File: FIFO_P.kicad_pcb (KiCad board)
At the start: 4 copper layers, 100 x 100 mm, 74 parts, among them J1 Vin +, J2 Vin -, J3 ICLK, J4 Vout, J5 Jack-DC, SW1 Rotary_Encoder_61C, U1 SN74LVC2G157_MUX_TI, U10 AD7840, U11 LM2776, U12 LM2940CT-5.0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

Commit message: Moved power
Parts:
- moved R2 15.4 mm to (91.5, 63.2), turned to 90 degrees
- moved JP2 13.5 mm to (118.0, 76.8), turned to 180 degrees
- moved R1 11.1 mm to (93.5, 63.2), turned to 90 degrees
- moved C20 11.0 mm to (66.5, 88.2)
- moved C21 11.0 mm to (66.5, 78.5)
- moved C22 11.0 mm to (66.5, 81.5)
- moved C25 11.0 mm to (77.2, 89.0)
- moved C26 11.0 mm to (66.5, 94.2)
- moved C27 11.0 mm to (80.2, 89.0)
- moved C28 11.0 mm to (66.5, 91.2)
- moved C29 11.0 mm to (66.5, 100.2)
- moved C30 11.0 mm to (66.5, 97.2)
- moved C31 11.0 mm to (85.8, 89.0)
- moved TP5 11.0 mm to (65.2, 85.0)
- moved TP6 11.0 mm to (92.5, 89.0)
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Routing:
- net Net-(C21-Pad1): track 34.3 -> 28.6 mm
- net -5V: track 183.2 -> 179.0 mm
- net +5V: track 225.8 -> 222.8 mm
- net GNDA: track 20.8 -> 17.8 mm
- net Net-(J2-Pad1): track 18.4 -> 19.6 mm
- net Net-(J1-Pad1): track 15.4 -> 16.6 mm
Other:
- board size 100 x 100 mm -> 95 x 100 mm
- board text added: "TODO {Non-,}differential signaling switch? Perfectly center traces between pins (where app.)? Silkscreen Check Soldermask Expansion Check Move power, reshape board: check Ard. stickout"
- board text removed: "TODO Extend SMD footprints {Non-,}differential signaling switch Center traces between pins Silkscreen Move power, reshape board: check Ard. stickout"

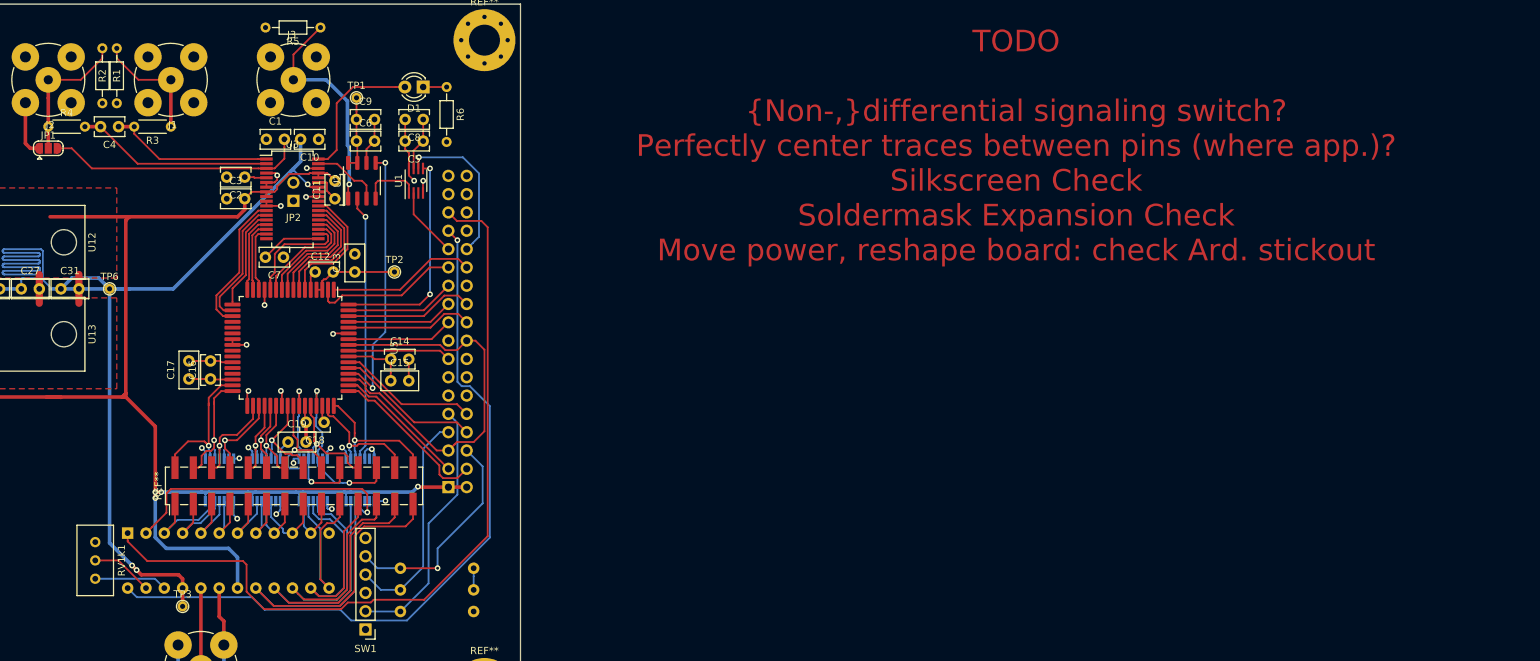
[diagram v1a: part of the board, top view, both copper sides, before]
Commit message: Actually fixed power and clocks
TODO: Flip arduino header and reroute
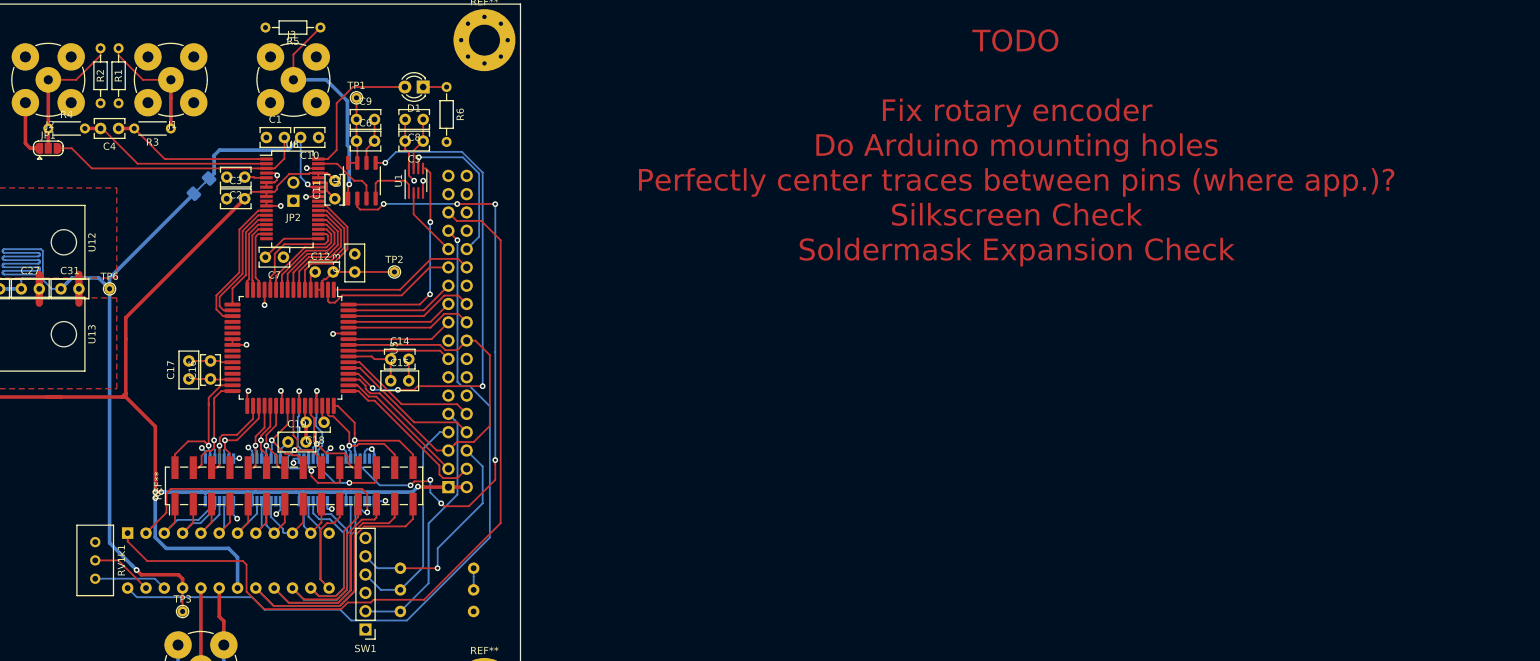
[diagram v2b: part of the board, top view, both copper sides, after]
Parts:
- added REF**: C_1206_3216Metric_Pad1.42x1.75mm_HandSolder, Capacitor_SMD:C_1206_3216Metric_Pad1.42x1.75mm_HandSolder, B.Cu at (105.2, 74.8)
- moved TP3 0.71 mm to (102.6, 133.8)
- moved C1 0.25 mm to (114.2, 68.0)
- moved C10 0.25 mm to (121.5, 68.0)
- moved C4 0.25 mm to (93.8, 66.8)
- moved R1 0.25 mm to (93.8, 63.2)
- moved R2 0.25 mm to (91.2, 63.2)
- moved R3 0.25 mm to (101.0, 66.8)
- moved R4 0.25 mm to (84.0, 66.8)
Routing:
- net LDAC: track 36.9 -> 84.2 mm, vias 1 -> 7
- net RCLK: track 38.7 -> 67.3 mm, vias 2 -> 4
- net +5V: track 222.8 -> 203.0 mm
- net -5V: track 179.0 -> 172.8 mm, vias 3 -> 2
- net Net-(U10-Pad1): track 110.7 -> 112.2 mm
- net Net-(C4-Pad1): track 22.9 -> 22.3 mm
- net Net-(U4-Pad24): track 56.4 -> 57.0 mm
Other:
- board text added: "TODO Fix rotary encoder Do Arduino mounting holes Perfectly center traces between pins (where app.)? Silkscreen Check Soldermask Expansion Check"
- board text removed: "TODO {Non-,}differential signaling switch? Perfectly center traces between pins (where app.)? Silkscreen Check Soldermask Expansion Check Move power, reshape board: check Ard. stickout"

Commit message: Fixed Arduino mounting holes
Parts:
- removed the REF** at (62.5, 71.0)
- added REF**: MountingHole_3.2mm_M3_ISO14580, MountingHole:MountingHole_3.2mm_M3_ISO14580, F.Cu at (60.8, 116.5)
- added REF**: MountingHole_3.2mm_M3_ISO14580, MountingHole:MountingHole_3.2mm_M3_ISO14580, F.Cu at (59.5, 68.2)
- moved REF** 5.00 mm to (54.5, 144.5)
- moved REF** 5.00 mm to (54.5, 54.5)
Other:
- board size 95 x 100 mm -> 100 x 100 mm
- board text added: "TODO Fix rotary encoder Perfectly center traces between pins (where app.)? Silkscreen Check Soldermask Expansion Check"
- board text removed: "TODO Fix rotary encoder Do Arduino mounting holes Perfectly center traces between pins (where app.)? Silkscreen Check Soldermask Expansion Check"

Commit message: Started silkscreen
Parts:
- removed the REF** at (54.5, 54.5)
- added M4: MountingHole_4.3mm_M4_Pad_Via, MountingHole:MountingHole_4.3mm_M4_Pad_Via, F.Cu at (54.5, 54.5)
- moved R5 11.1 mm to (111.0, 55.7), turned to 270 degrees
- moved TP4 7.92 mm to (65.6, 67.5)
- moved SW1 1.00 mm to (128.0, 137.2)
- moved R8 0.34 mm to (142.7, 134.0)
- moved R7 0.28 mm to (142.7, 130.8)
- moved R9 0.26 mm to (142.7, 127.7)
- renumbered REF** to M4
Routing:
- net Net-(U10-Pad1): track 112.2 -> 114.3 mm
- net Net-(R9-Pad2): track 30.5 -> 28.5 mm
- net 3.3V: track 89.4 -> 87.6 mm
- net Net-(U10-Pad24): track 102.5 -> 103.3 mm
- net Net-(J3-Pad1): track 31.2 -> 31.8 mm
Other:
- board text added: "3.3V"
- board text added: "Clock"
- board text added: "Differential Inputs"
- board text added: "Input Overflow"
- board text added: "Short to GND"
- board text removed: "APPROX"

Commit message: Silkscreen cleaned up on both sides
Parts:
- removed the REF** at (59.5, 68.2)
- added M3: MountingHole_3.2mm_M3_ISO14580, MountingHole:MountingHole_3.2mm_M3_ISO14580, F.Cu at (59.5, 68.2)
- moved TP7 1.69 mm to (66.5, 105.2)
- moved R6 1.50 mm to (140.8, 61.0)
- moved JP1 1.25 mm to (84.0, 70.8)
- renumbered REF** to M3
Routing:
- net GND: track 83.8 -> 79.1 mm
- net 3.3V: track 87.6 -> 89.3 mm
- net Net-(D1-Pad1): track 3.31 -> 4.75 mm
- net Net-(J2-Pad1): track 19.1 -> 20.4 mm
- net GNDA: track 17.8 -> 18.4 mm
- net Net-(C1-Pad2): track 36.1 -> 35.6 mm
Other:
- board text added: "+5V"
- board text added: "-5V"
- board text added: "-5V Charge Pump"
- board text added: "ADC"
- board text added: "Arduino Due"
- board text added: "Clock Buffer"
- board text added: "D0"
- board text added: "D13"
- board text added: "DAC"
- board text added: "DAC In"
- board text added: "Delay Adjust"
- board text added: "Delayed Output"
- board text added: "FIFO"
- board text added: "FIFO Out"
- board text added: "Ferrite or Short"
- board text added: "G N D"
- board text added: "GND"
- board text added: "GNDA"
- board text added: "MUX"
- board text added: "Q17"
- board text added: "Q4"
- board text added: "Reference Adjust"
- board text added: "Vin"
- board text added: "a"
- board text added: "b"
- board text added: "c"
- board text removed: "TODO Fix rotary encoder Perfectly center traces between pins (where app.)? Silkscreen Check Soldermask Expansion Check"

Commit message: More tweaks
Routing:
- net LDAC: track 84.2 -> 88.7 mm
- net Net-(R7-Pad2): track 30.6 -> 29.9 mm
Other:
- board text added: "Cut before +ferrite"
- board text removed: "Ferrite or Short"

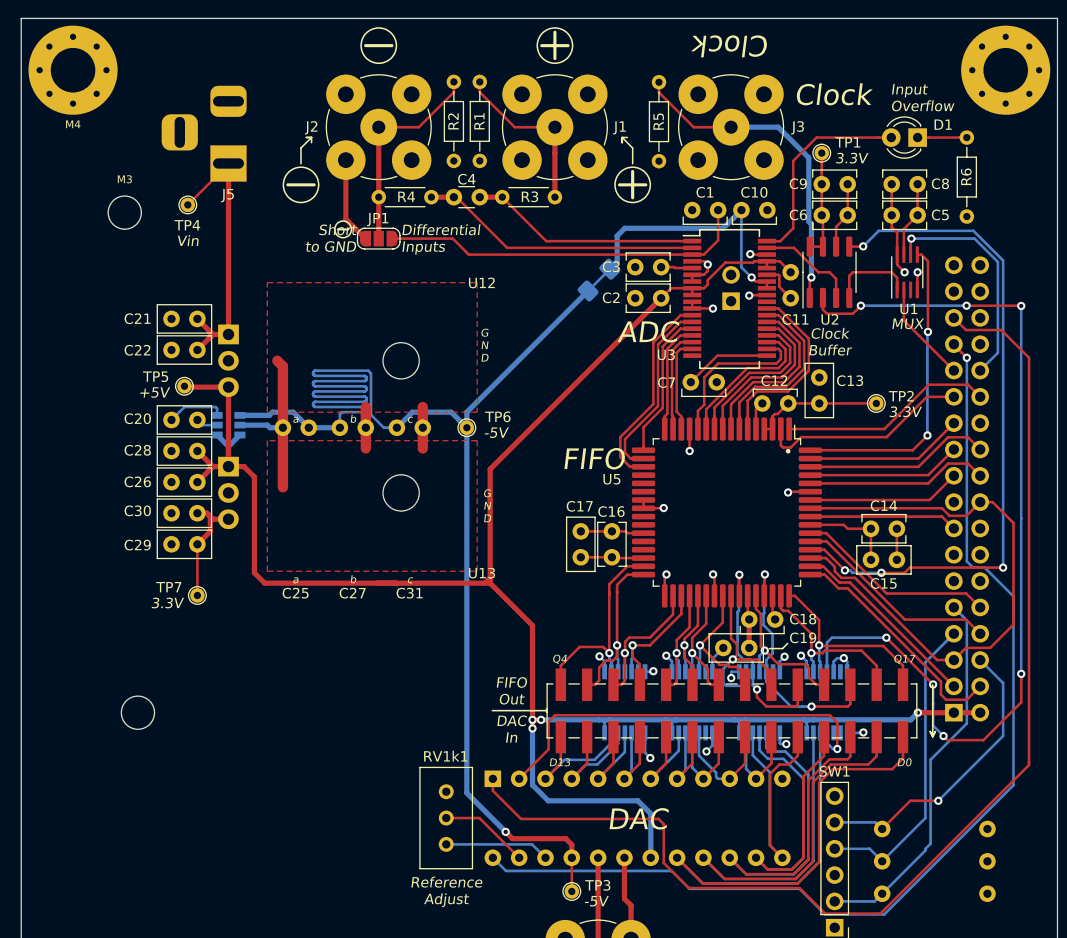
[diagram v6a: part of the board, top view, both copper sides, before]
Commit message: Added screw terminal footprint
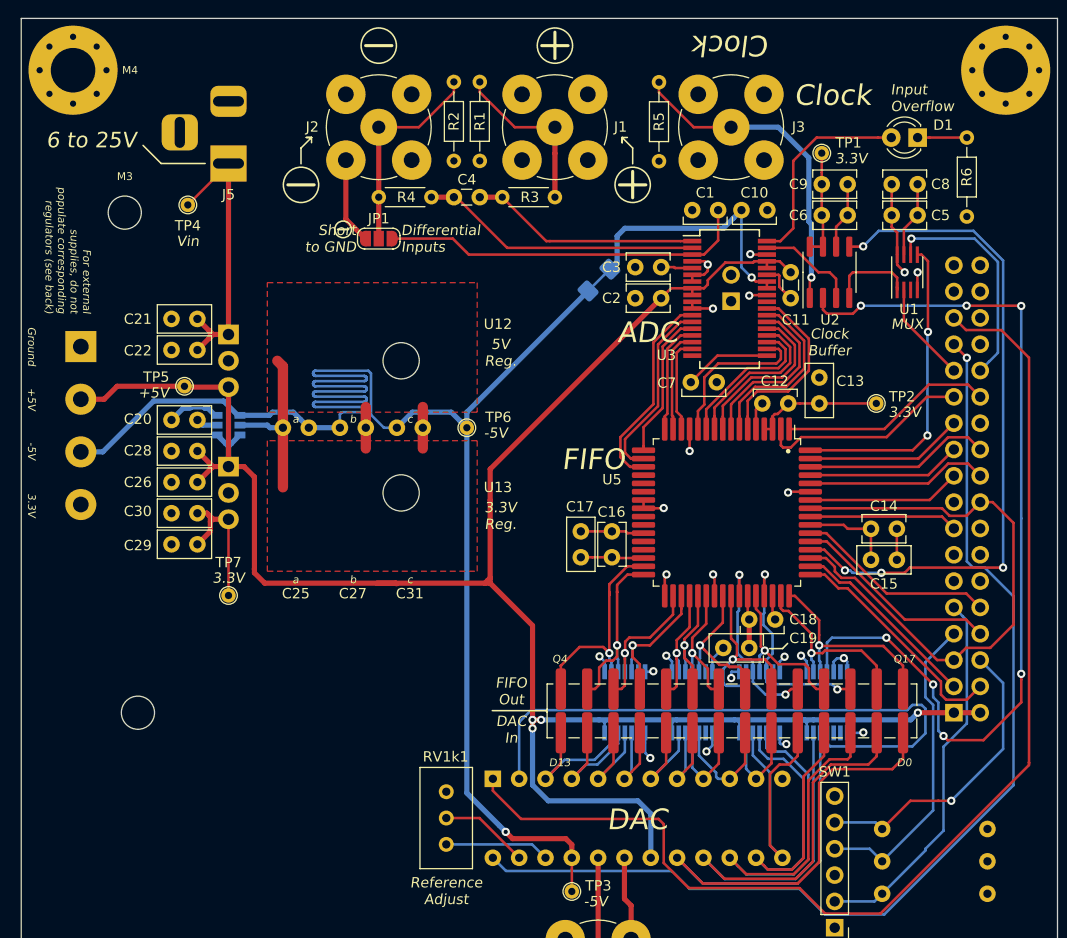
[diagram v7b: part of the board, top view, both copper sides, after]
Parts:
- added REF**: TerminalBlock_bornier-4_P5.08mm, TerminalBlock:TerminalBlock_bornier-4_P5.08mm, F.Cu at (55.2, 81.2)
- REF**: value PinHeader_2x14_P2.54mm_Vertical_SMD -> SolderJumper_PinHeader_2x14_P2.54mm_Vertical_SMD; footprint Connector_PinHeader_2.54mm:PinHeader_2x14_P2.54mm_Vertical_SMD -> FIFO_P:SolderJumper_PinHeader_2x14_P2.54mm_Vertical_SMD
- moved TP7 3.00 mm to (69.5, 105.2)
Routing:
- net LDAC5V: track 39.9 -> 59.0 mm, vias 1 -> 0
- net -5V: track 172.8 -> 190.8 mm
- net +5V: track 203.0 -> 213.5 mm
- net Net-(U5-Pad42): track 21.4 -> 18.5 mm
- net Net-(U5-Pad45): track 24.5 -> 21.8 mm
- net Net-(U5-Pad40): track 15.3 -> 17.7 mm
- net 3.3V: track 89.3 -> 91.7 mm
- net Net-(U5-Pad41): track 18.0 -> 19.9 mm
- net Net-(R9-Pad2): track 28.5 -> 29.2 mm
- net Net-(R7-Pad2): track 29.9 -> 30.5 mm
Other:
- board text added: "+5V Ext."
- board text added: "-5V CP (back)"
- board text added: "-5V Ext."
- board text added: "3.3V Ext."
- board text added: "3.3V Reg."
- board text added: "5V Reg."
- board text added: "6 to 25V"
- board text added: "For external supplies, do not populate corresponding regulators (see back)"
- board text added: "Ground"
- board text removed: "G N D"

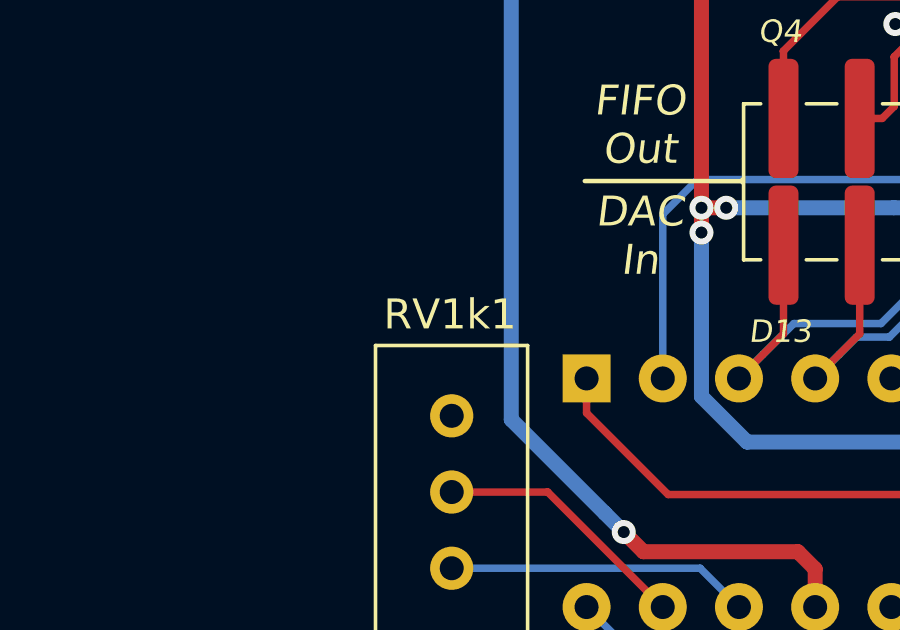
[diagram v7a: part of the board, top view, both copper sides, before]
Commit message: Fixed RV refdes
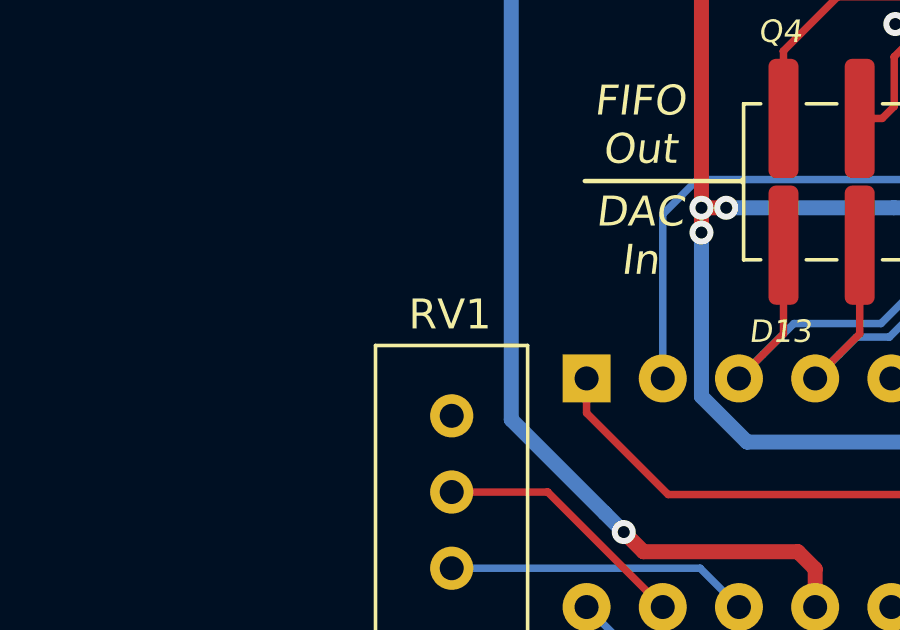
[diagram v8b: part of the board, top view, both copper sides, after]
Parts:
- renumbered RV1k1 to RV1
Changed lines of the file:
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@@
     (descr "Potentiometer, vertical, Bourns 3296W, https://www.bourns.com/pdfs/3296.pdf")
     (tags "Potentiometer vertical Bourns 3296W")
-    (fp_text reference RV1k1 (at -8.456 0.057 180) (layer F.SilkS)
+    (fp_text reference RV1 (at -8.456 0.057 180) (layer F.SilkS)
       (effects (font (size 1 1) (thickness 0.15)))
     )
